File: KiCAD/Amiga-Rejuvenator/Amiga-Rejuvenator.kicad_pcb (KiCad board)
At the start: 4 copper layers, 241.8 x 174.8 mm, 120 parts, among them J1 GND, J15 28M, J17 RMBCLKS, J18 GND, J19 +12X, U1 74LS245, U10 V53C104, U11 V53C104, U12 V53C104, U13 V53C104, U14 74LS244-U16,U17, U15 74LS373, U16 74LS244-U16,U17, U17 74LS244-U16,U17, U18 512K-ROM, U19 8372-FatAgnus, U19B1 8361-Agnus, U2 74LS393-U2, U20 8364-Paula, U20B1 8364-Paula, U21 74LS245, U22 74LS245, U23 RP, U24 RP, U25 8362-Denise, U25B1 8362-Denise, U26 74HC245, U27 OKI6242B, U28 PAL16L8, U29 PAL16L8, U3 74F257, U30 PAL20L8, U31 PAL20L8, U32 74LS74, U33 74LS04, U34 74HC245, U35 74F257, U36 PALCAS, U37 PALEN, U38 U3I, U39 U3G, U4 74LS244-U16,U17, U40 U2J, U41 U2I, U5 74LS373, U6 V53C104, U7 V53C104, U8 V53C104, U9 V53C104, X1 X1, X14 X14, X15 X15, X16 VideoSlot 1, X17 VideoSlot 2, Y1 Crystal

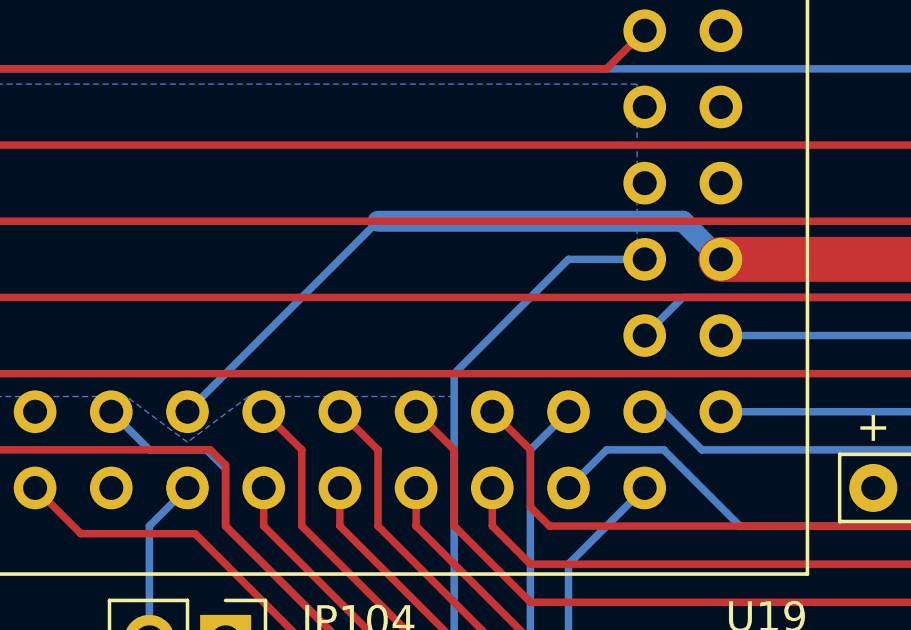
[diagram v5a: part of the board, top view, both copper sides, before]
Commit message: Power plane update
Eliminated redundant tracks placed inside fill zones.
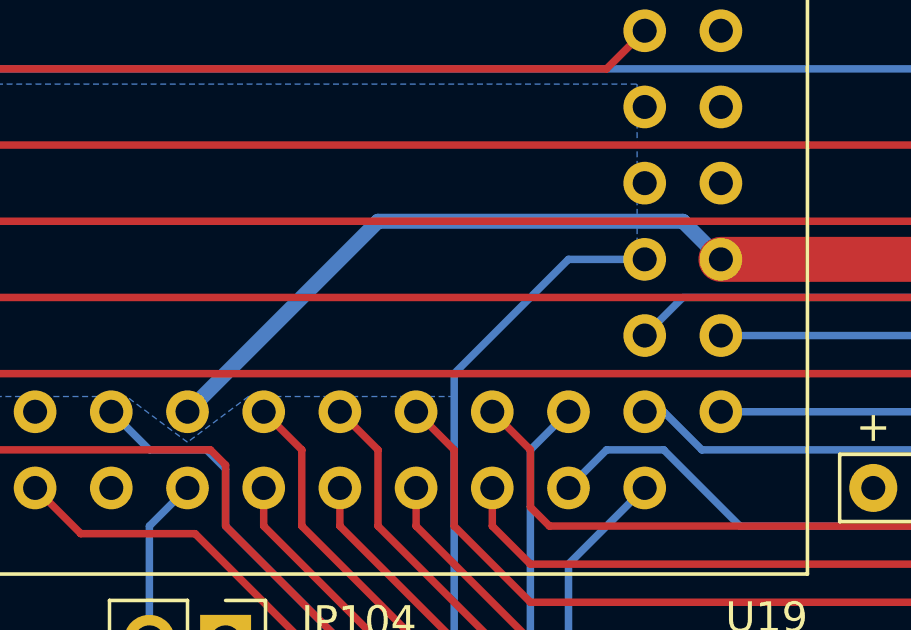
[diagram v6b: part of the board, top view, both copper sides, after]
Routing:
- net GND: track 629.9 -> 591.2 mm

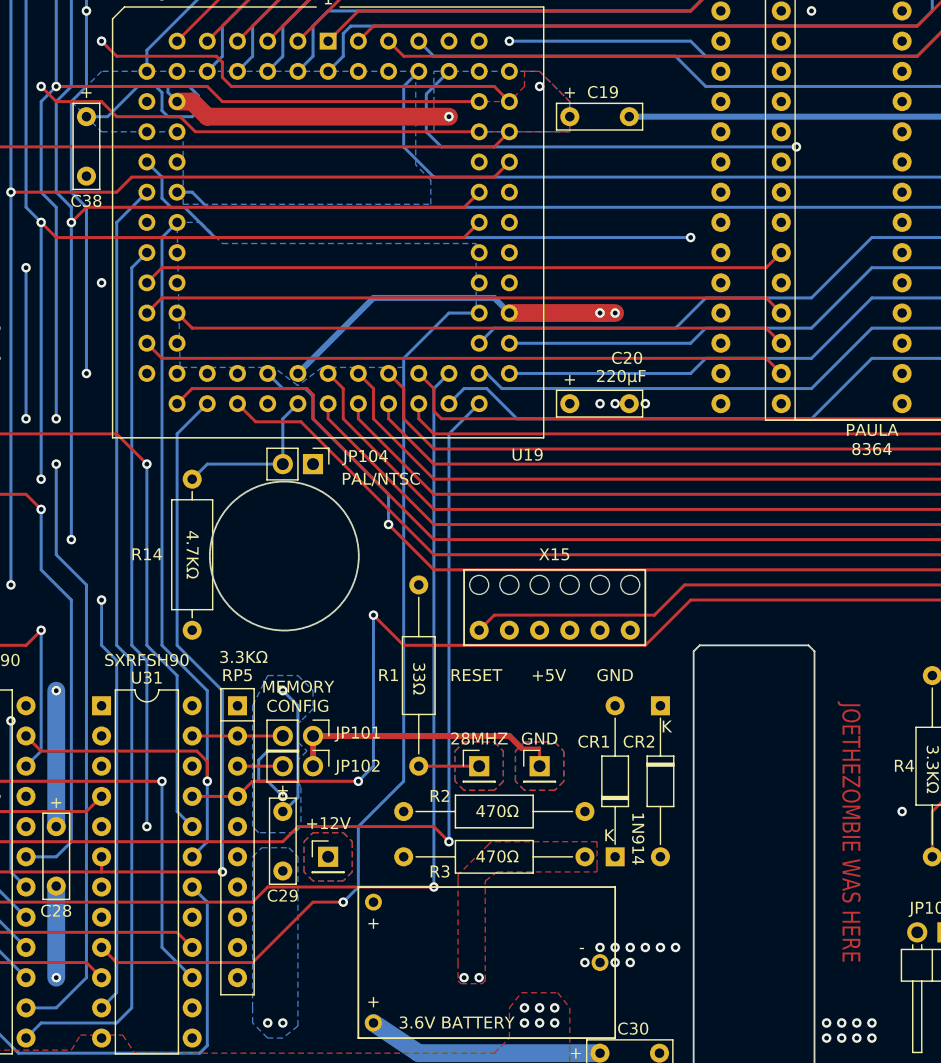
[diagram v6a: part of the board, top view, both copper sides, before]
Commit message: Add directional signals for Agnus.  Add PWR_FLAG for power inputs.
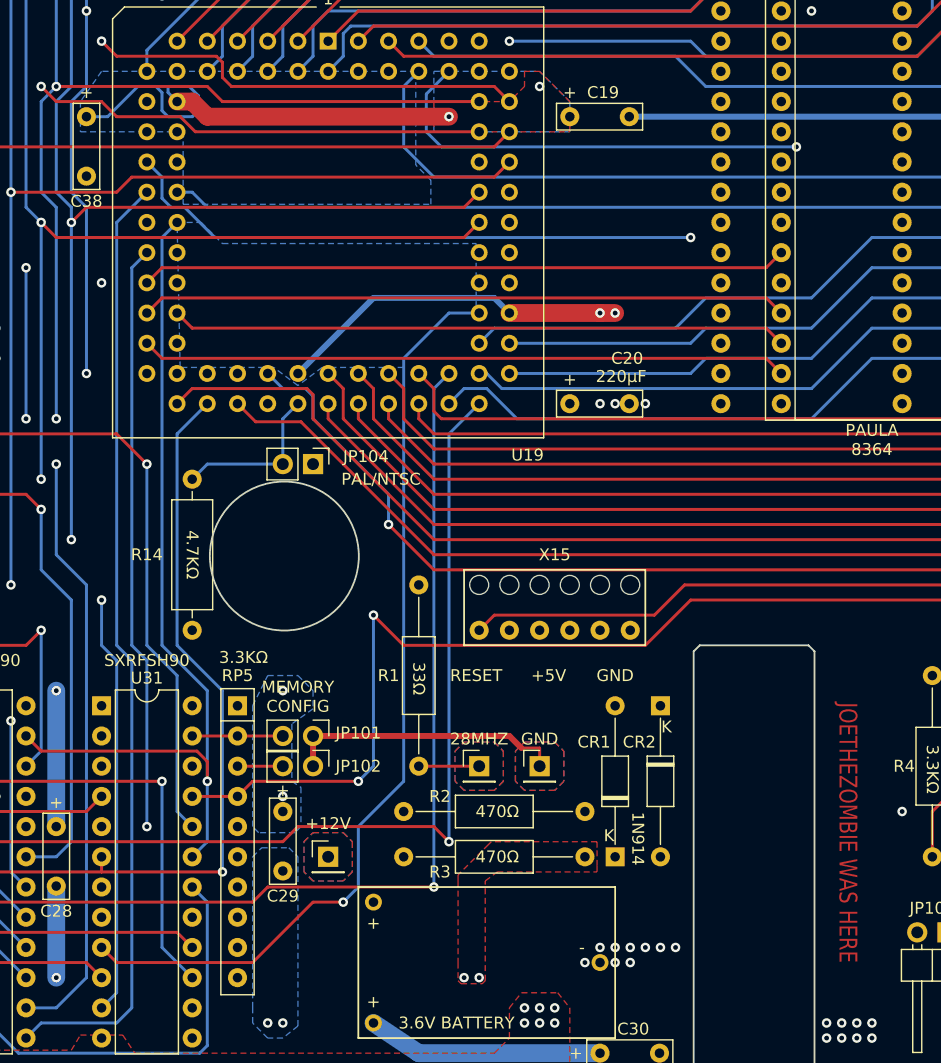
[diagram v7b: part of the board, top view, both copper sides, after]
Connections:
- net Net-(BT1-Pad1) renamed +BATT
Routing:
- net +5V: track 383.4 -> 364.1 mm
- net GND: track 591.2 -> 588.4 mm

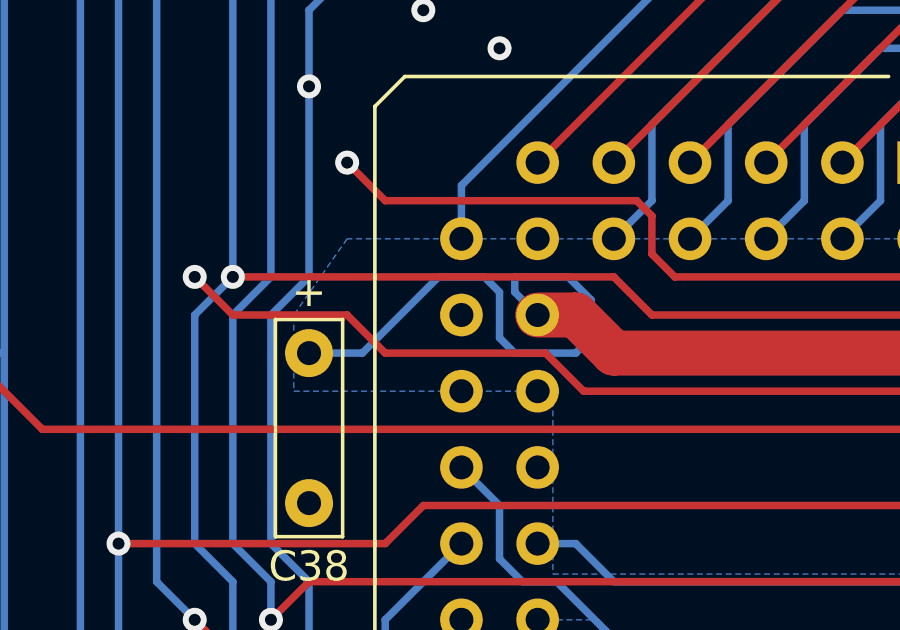
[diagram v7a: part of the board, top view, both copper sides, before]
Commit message: Signaling Update
Updated signal direction for RAM, custom chips, and motherboard headers.  Rejuvenator now completes the ERC check error free!  (It previously had errors due to missing signal directions on the symbol entries.)

Renamed nets that are connected by way of the mainboard.  Previously, these nets were named (for example) X2.~CDW, X9.~CDW, X15.~CDW.  Now these same signals would be named ~CDWa, ~CDWb, ~CDWc.   Keep in mind, these are all the same signal.  They are not connected on the rejuvenator itself, but they become interconnected once plugged to the mainboard.  For example, all the CDWa,b,c signals are the same CDW signal, just fed up to Rejuvenator from different points on the mainboard.
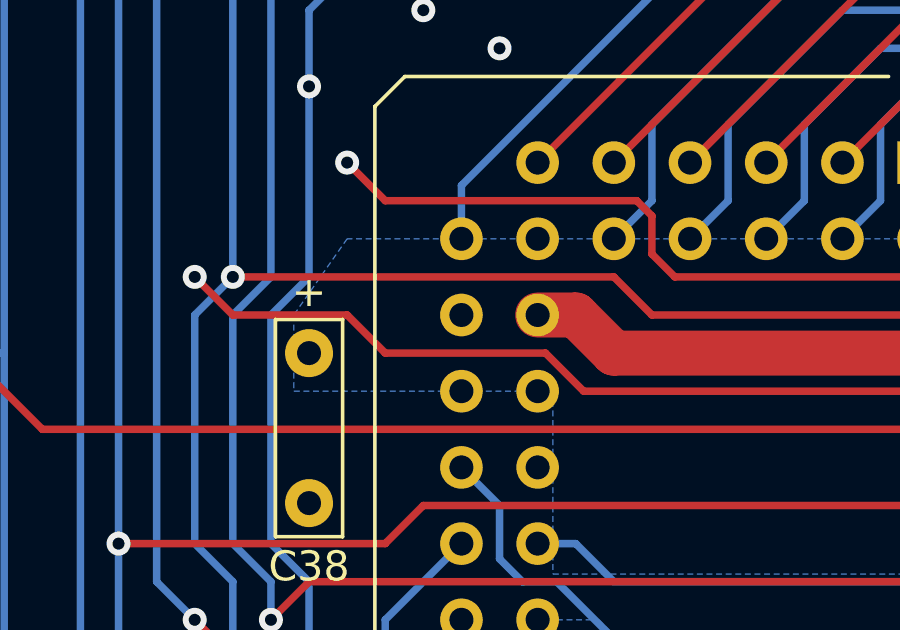
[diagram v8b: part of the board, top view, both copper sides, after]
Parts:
- U19B1: value 8361-Agnus -> 8361-Agnus-Socket
- U20B1: value 8364-Paula -> 8364-Paula-Socket
- U25B1: value 8362-Denise -> 8362-Denise-Socket
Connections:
- net +BATT renamed Net-(BT1-Pad1)
- net /BATT+ renamed Net-(C23-Pad1)
- net /X2.C4 renamed /C4b
- net /X3.~RE renamed /~RE~b
- net /X5.~RE renamed /~RE~c
- net /X6.~CDW renamed /~CDW~b
- net /X7.~CDW renamed /~CDW~c
- net /X8.~CDW renamed /~CDW~d
- net /X9.~CDW renamed /~CDW~e
- net Net-(J19-Pad1) renamed +12V
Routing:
- net +5V: track 364.1 -> 345.8 mm
